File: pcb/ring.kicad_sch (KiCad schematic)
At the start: 64 parts, among them IC1 EFR32BG27C140F768IM32-B, J1 Conn_Coaxial_Small, Q2 CSD13380F3, Q3 CSD13380F3, U1 TMP117xxDRV, U2 TPS7A20xxxDQN, U3 LSM6DSOXTR, U4 MAX30102, U5 BQ297xy, U6 BQ27427YZFR, Y2 38.4MHz

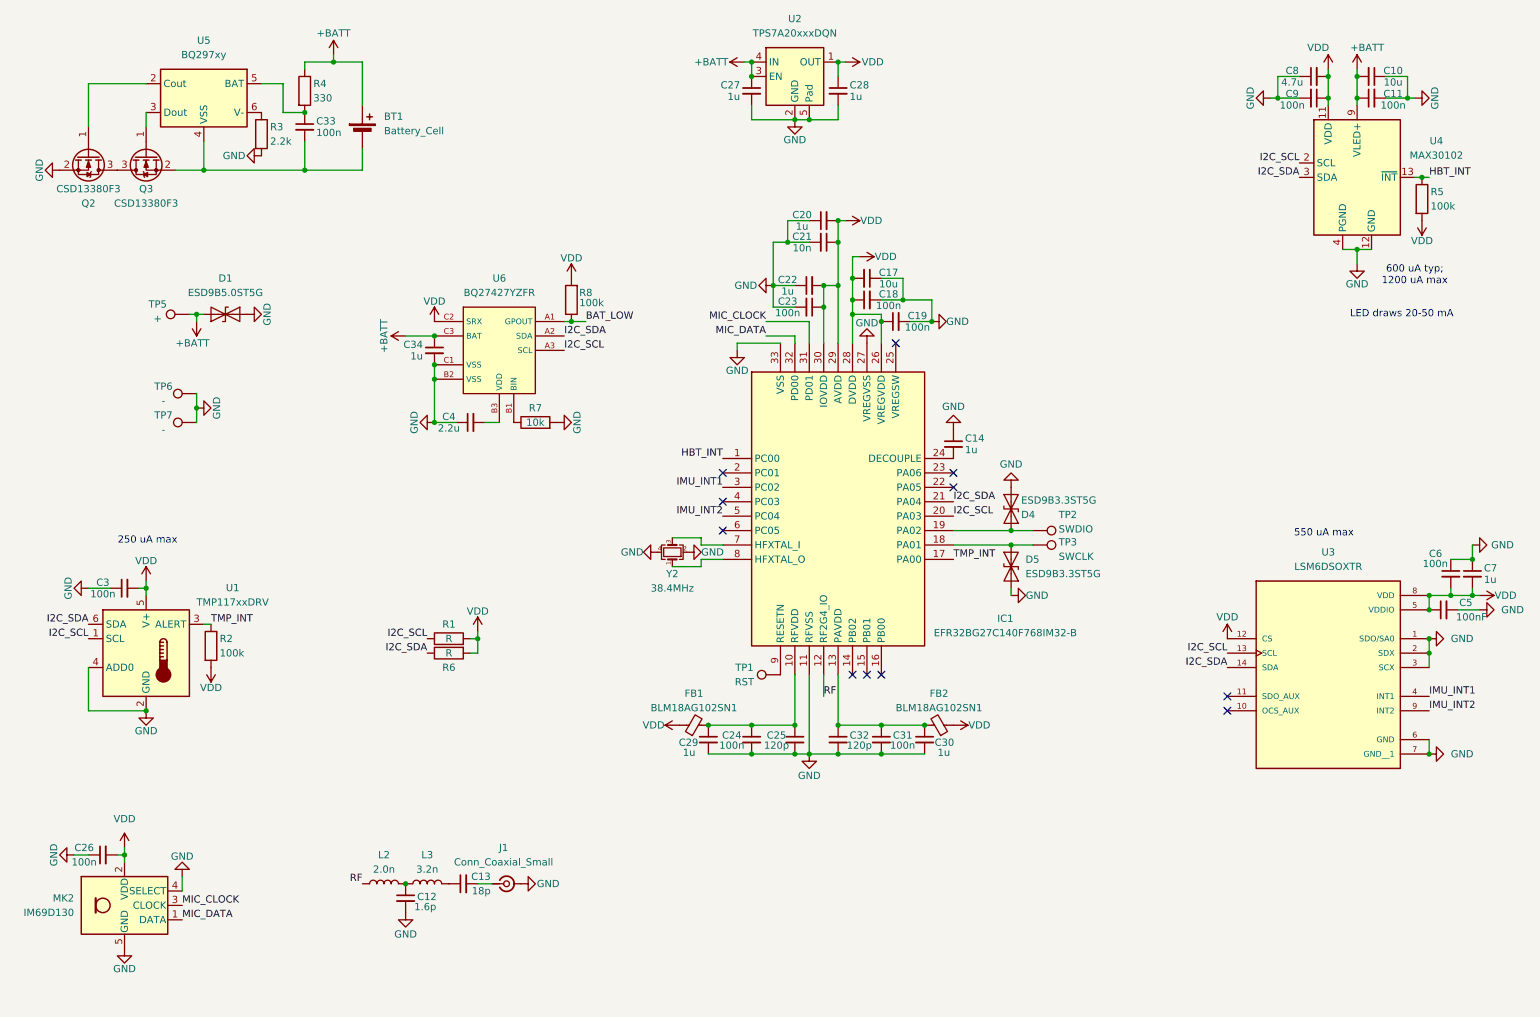
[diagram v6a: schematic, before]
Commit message: nearly done routing
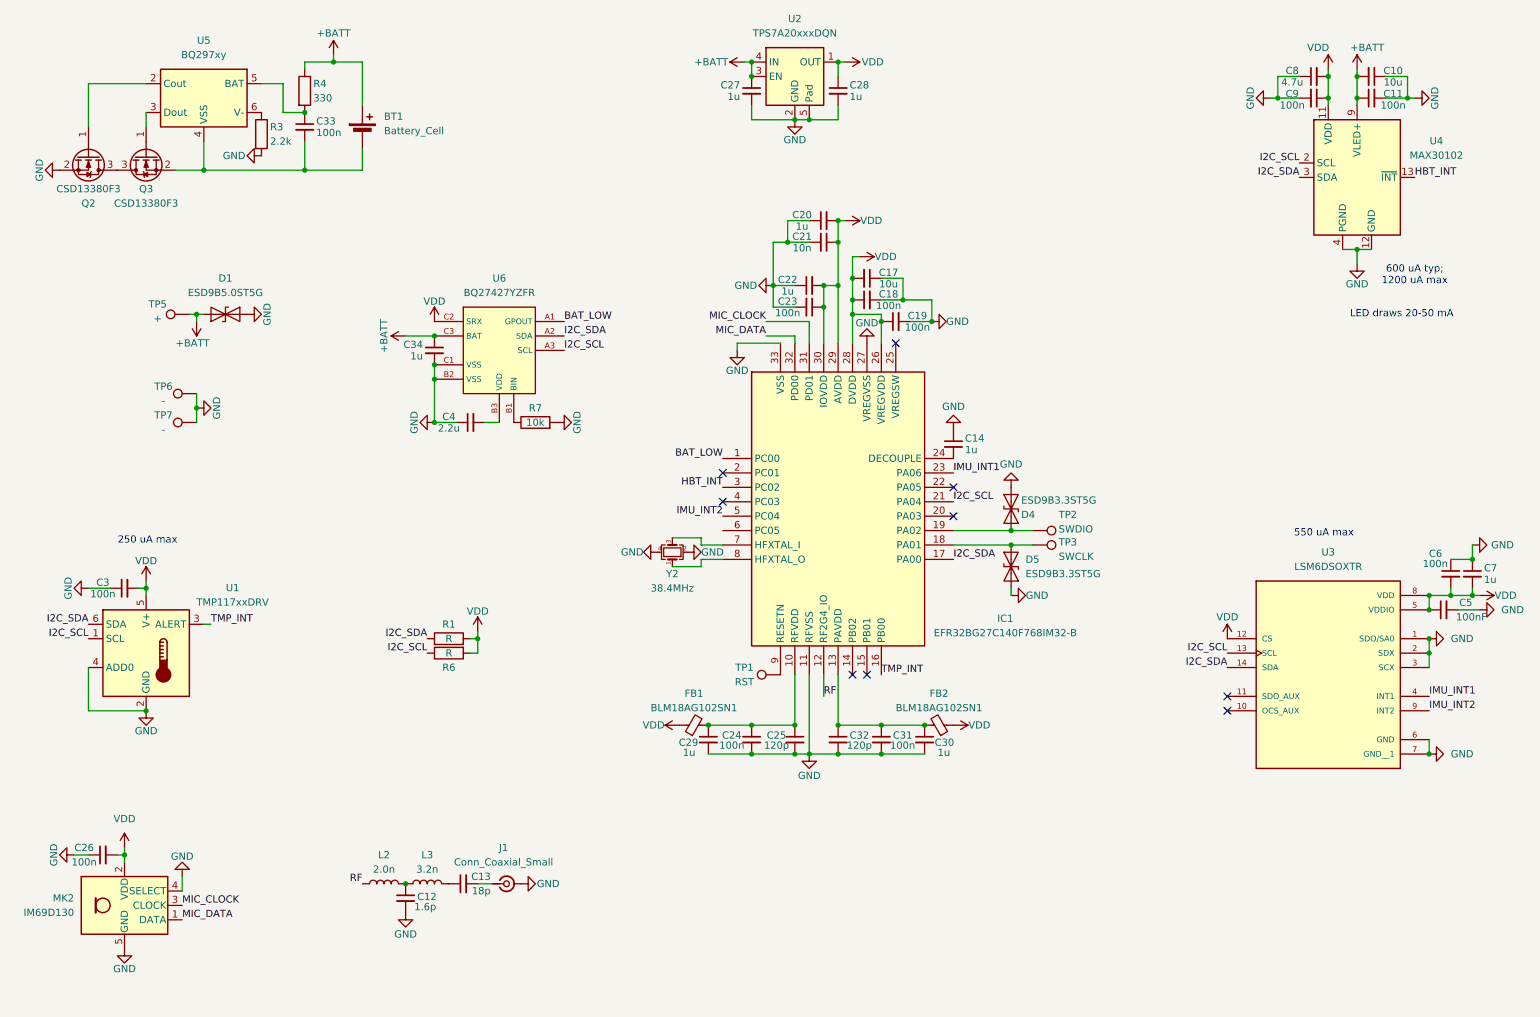
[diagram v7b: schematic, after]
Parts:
- removed R2, R5, R8: 100k, Resistor_SMD:R_0201_0603Metric, symbol Device:R
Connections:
- net BAT_LOW: now also IC1.1 (PC00)
- net HBT_INT: now also IC1.3 (PC02); no longer IC1.1 (PC00)
- net I2C_SCL: now also IC1.21 (PA04), R6.1; no longer IC1.20 (PA03), R1.1
- net I2C_SDA: now also IC1.17 (PA00), R1.1; no longer IC1.21 (PA04), R6.1
- net IMU_INT1: now also IC1.23 (PA06); no longer IC1.3 (PC02)
- net TMP_INT: now also IC1.16 (PB00); no longer IC1.17 (PA00)
- no-connect marks 11 -> 9
